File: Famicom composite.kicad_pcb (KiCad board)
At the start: 2 copper layers, 33.3 x 17 mm, 13 parts, among them J1 PPU_Pin21, J2 Conn_01x02, J3 Audio_In, J4 Conn_01x04_Female, Q1 Q_NJFET_GSD, Q2 Q_PJFET_GSD

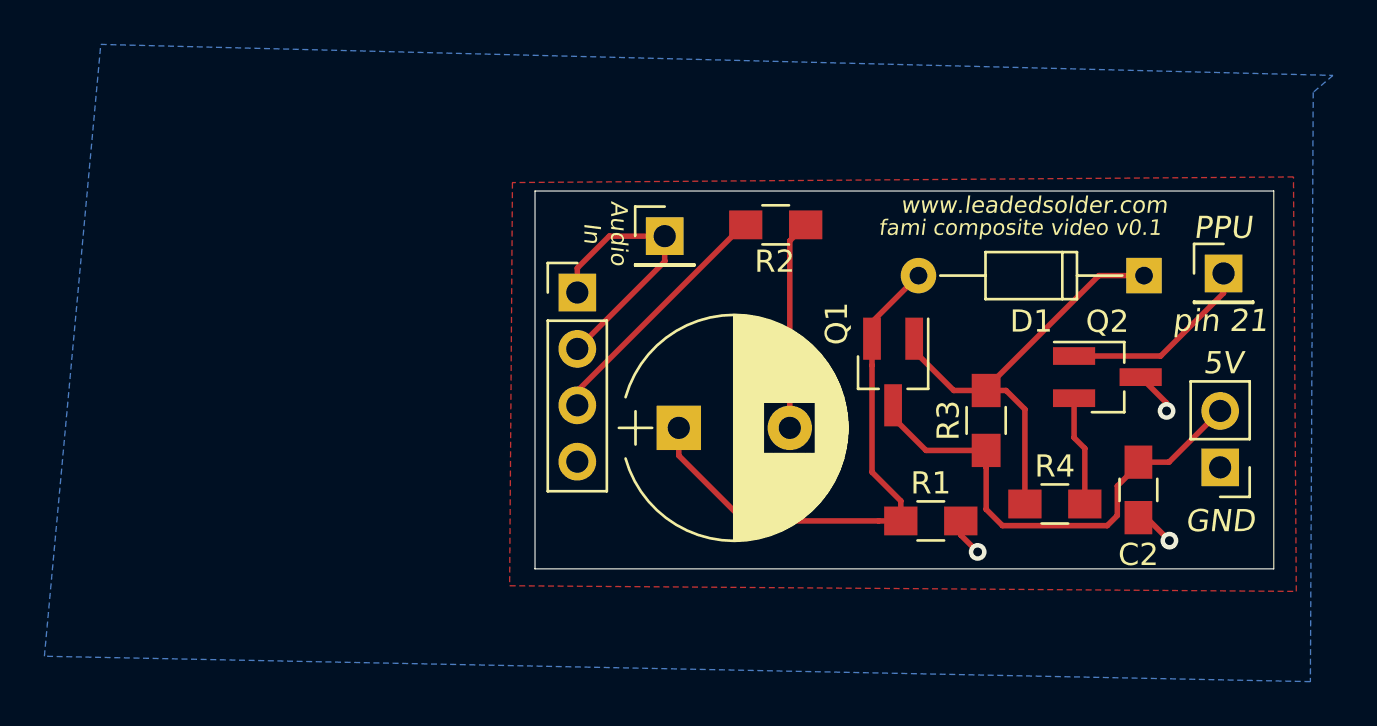
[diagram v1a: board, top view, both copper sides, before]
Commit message: THS7314 analogue video amp version
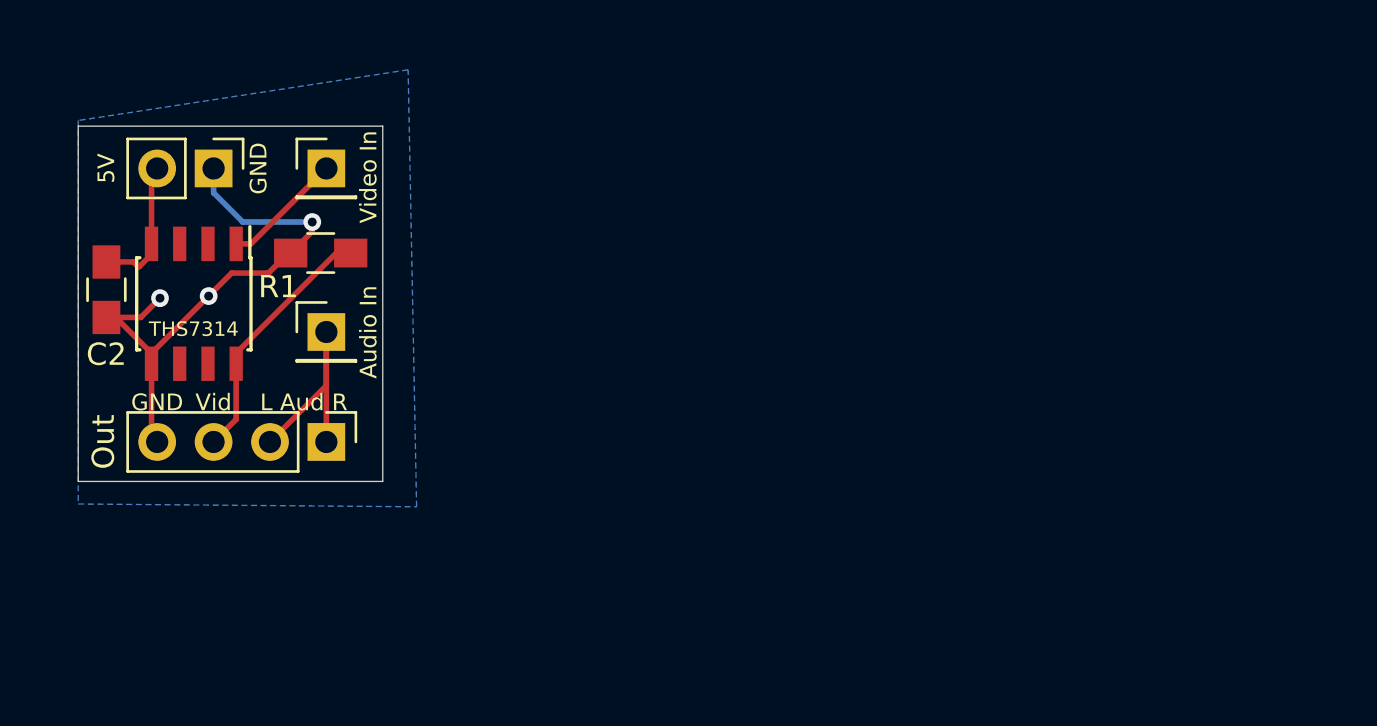
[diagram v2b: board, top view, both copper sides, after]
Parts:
- removed C1: 220µF, Capacitors_ThroughHole:CP_Radial_D10.0mm_P5.00mm
- removed D1: 1n4148, Diodes_ThroughHole:D_DO-35_SOD27_P10.16mm_Horizontal
- removed Q1: Q_NJFET_GSD, TO_SOT_Packages_SMD:SOT-23_Handsoldering
- removed Q2: Q_PJFET_GSD, TO_SOT_Packages_SMD:SOT-23_Handsoldering
- removed R2: 82Ω, Resistors_SMD:R_0805_HandSoldering
- removed R3: 2200Ω, Resistors_SMD:R_0805_HandSoldering
- removed R4: 220Ω, Resistors_SMD:R_0805_HandSoldering
- added U1: THS7314, Housings_SOIC:SOIC-8_3.9x4.9mm_Pitch1.27mm, F.Cu at (133.9, 91.9)
- R1: value 68Ω -> 1kΩ
- moved C2 47.3 mm to (129.9, 91.3)
- moved J2 47.3 mm to (134.7, 85.9), turned to 270 degrees
- moved J1 40.7 mm to (139.8, 85.9)
- moved R1 30.0 mm to (139.6, 89.7)
- moved J3 15.8 mm to (139.8, 93.2)
- moved J4 13.2 mm to (139.8, 98.2), turned to 270 degrees
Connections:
- J1 pad 1: /B -> Net-(J1-Pad1)
- R1 pad 1: Net-(C1-Pad1) -> GND
- R1 pad 2: GND -> /Vid_Out
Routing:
- net Net-(C1-Pad1): track 24.9 -> 0.00 mm
- net Net-(D1-Pad1): track 20.3 -> 0.00 mm
- net GND: track 5.88 -> 26.0 mm
- net +5V: track 22.6 -> 6.32 mm
- net Net-(C1-Pad2): track 9.44 -> 0.00 mm
- net /B: track 8.79 -> 0.00 mm
- net Net-(J1-Pad1): track 0.00 -> 5.47 mm
- net /E: track 4.97 -> 0.00 mm
- net Net-(J3-Pad1): track 12.3 -> 11.0 mm
- removed copper zone on F.Cu, net GND
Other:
- board size 33.3 x 17 mm -> 13.7 x 16 mm
- board text added: "L Aud R"
- board text added: "Out"
- board text added: "THS7314"
- board text added: "Vid"
- board text added: "Video In"
- board text added: "fami composite v0.2"
- board text added: "leadedsolder.com 2020"
- board text removed: "Ground"
- board text removed: "Left Audio"
- board text removed: "PPU"
- board text removed: "Right Audio"
- board text removed: "Video"
- board text removed: "fami composite video v0.1"
- board text removed: "www.leadedsolder.com"

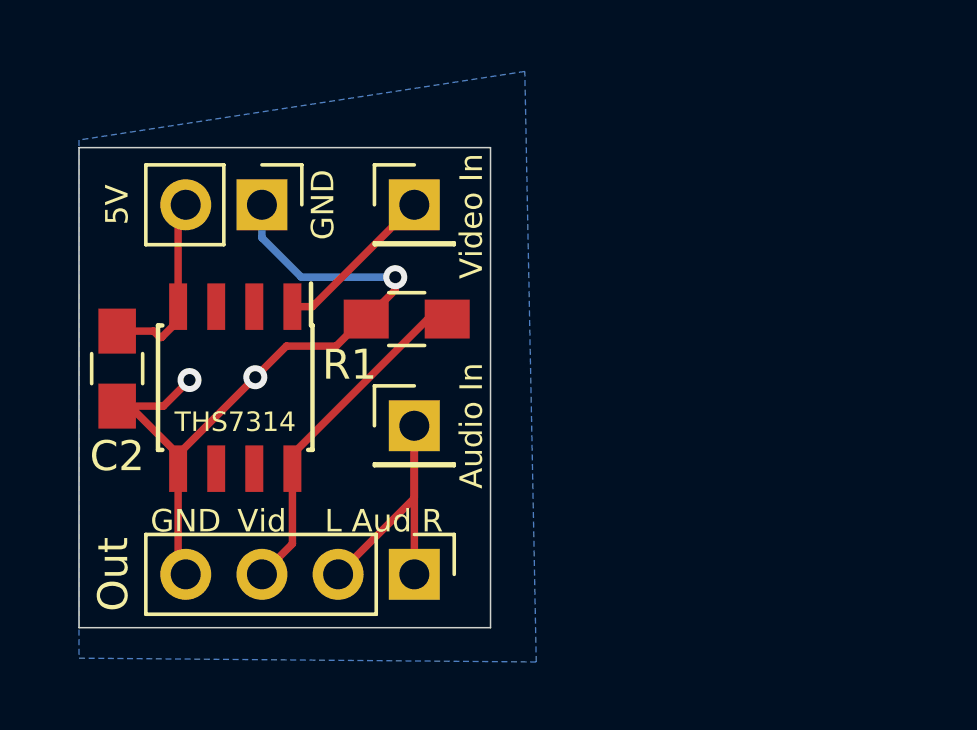
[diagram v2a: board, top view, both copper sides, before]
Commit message: v0.3 - 75ohm attenuation, video filter cap
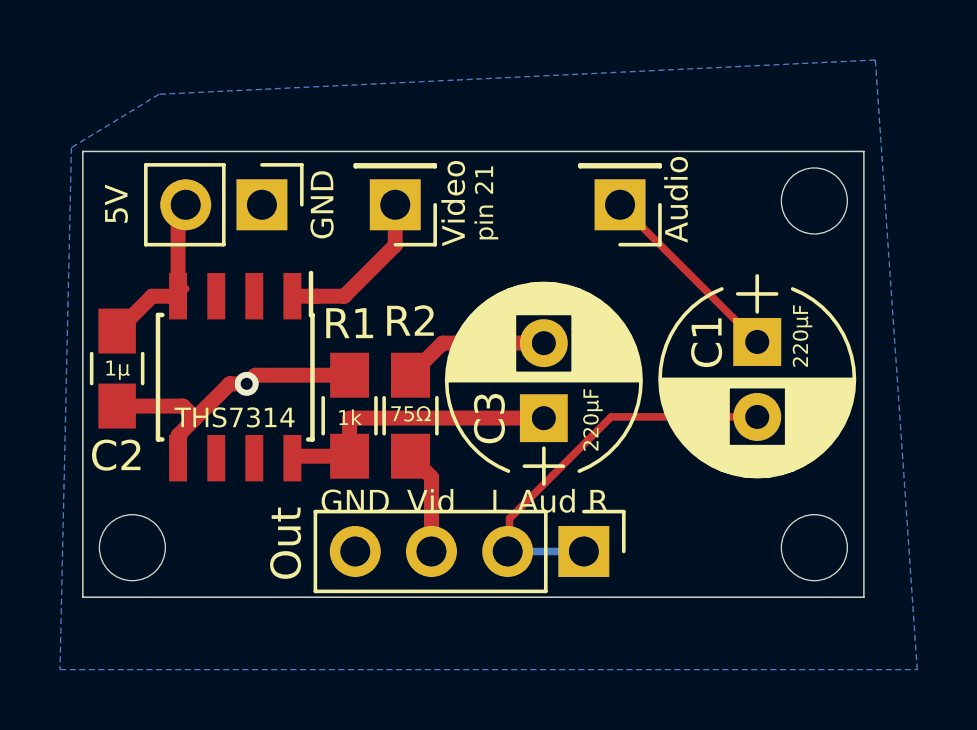
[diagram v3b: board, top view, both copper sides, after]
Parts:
- added C1: 220µF, Capacitors_ThroughHole:CP_Radial_D6.3mm_P2.50mm, F.Cu at (151.3, 90.4)
- added C3: 330µF, Capacitors_ThroughHole:CP_Radial_D6.3mm_P2.50mm, F.Cu at (144.1, 93.0)
- added R2: 75Ω, Resistors_SMD:R_0805_HandSoldering, F.Cu at (139.7, 92.9)
- added REF**: MountingHole_2.2mm_M2_DIN965, Mounting_Holes:MountingHole_2.2mm_M2_DIN965, F.Cu at (130.4, 97.3)
- added REF**: MountingHole_2.2mm_M2_DIN965, Mounting_Holes:MountingHole_2.2mm_M2_DIN965, F.Cu at (153.2, 97.3)
- added REF**: MountingHole_2.2mm_M2_DIN965, Mounting_Holes:MountingHole_2.2mm_M2_DIN965, F.Cu at (153.2, 85.7)
- added REF***: OSHW-Logo2_9.8x8mm_SilkScreen, Symbols:OSHW-Logo2_9.8x8mm_SilkScreen, B.Cu at (134.2, 92.3)
- moved J3 10.1 mm to (146.7, 85.9), turned to 180 degrees
- moved J4 5.70 mm to (145.5, 97.4)
- moved R1 3.74 mm to (137.7, 92.9), turned to 270 degrees
- moved J1 0.63 mm to (139.2, 85.9), turned to 180 degrees
- moved U1 0.35 mm to (133.9, 91.6)
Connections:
- J3 pad 1: Net-(J3-Pad1) -> Net-(C1-Pad1)
- J4 pad 1: Net-(J3-Pad1) -> Net-(C1-Pad2)
- J4 pad 2: Net-(J3-Pad1) -> Net-(C1-Pad2)
- R1 pad 2: /Vid_Out -> Net-(C3-Pad1)
- U1 pad 8: /Vid_Out -> Net-(C3-Pad1)
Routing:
- net GND: track 26.0 -> 10.6 mm, vias 3 -> 1
- net Net-(C1-Pad2): track 0.00 -> 13.3 mm
- net Net-(J3-Pad1): track 11.0 -> 0.00 mm
- net Net-(C3-Pad1): track 0.00 -> 9.77 mm
- net /Vid_Out: track 11.4 -> 3.46 mm
- net Net-(C1-Pad1): track 0.00 -> 6.47 mm
- net Net-(C3-Pad2): track 0.00 -> 4.89 mm
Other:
- board size 13.7 x 16 mm -> 26 x 14.9 mm
- board text added: "1k"
- board text added: "1µ"
- board text added: "220µF"
- board text added: "75Ω"
- board text added: "Audio"
- board text added: "Video"
- board text removed: "Audio In"
- board text removed: "Video In"
- board text removed: "fami composite v0.2"

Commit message: add input-side cap, ground other inputs
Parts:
- added C4: 0.1µF, Capacitor_SMD:C_0805_2012Metric_Pad1.15x1.40mm_HandSolder, F.Cu at (138.7, 89.2)
- moved J4 3.11 mm to (148.6, 97.4)
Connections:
- J1 pad 1: Net-(J1-Pad1) -> Net-(C4-Pad2)
- U1 pad 1: Net-(J1-Pad1) -> Net-(C4-Pad1)
- U1 pad 2: Net-(U1-Pad2) -> GND
- U1 pad 3: Net-(U1-Pad3) -> GND
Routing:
- net GND: track 10.6 -> 16.4 mm
- net Net-(J1-Pad1): track 5.48 -> 0.00 mm
- net Net-(C1-Pad2): track 13.3 -> 8.13 mm
- net Net-(C4-Pad2): track 0.00 -> 3.52 mm
- net Net-(C4-Pad1): track 0.00 -> 2.00 mm
- net /Vid_Out: track 3.46 -> 5.43 mm
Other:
- board text added: "famicom composite board v0.4"
